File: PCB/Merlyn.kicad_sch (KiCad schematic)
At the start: 92 parts, among them J1 Conn_Coaxial_Small, Q1 JMSL0302AU, Q10 JMSL0302AU, Q11 JMSL0302AU, Q12 JMSL0302AU, Q13 JMSL0302AU, Q14 JMSL0302AU, Q15 JMSL0302AU, Q16 JMSL0302AU, Q17 JMSL0302AU, Q18 JMSL0302AU, Q19 JMSL0302AU, Q2 JMSL0302AU, Q20 JMSL0302AU, Q21 JMSL0302AU, Q22 JMSL0302AU, Q23 JMSL0302AU, Q24 JMSL0302AU, Q3 JMSL0302AU, Q4 JMSL0302AU, Q5 JMSL0302AU, Q6 JMSL0302AU, Q7 JMSL0302AU, Q8 JMSL0302AU, Q9 JMSL0302AU, U1 AT32F435CGU7, U10 JSM6288Q, U11 EFM8BB21F16G-C-QFN20, U12 EFM8BB21F16G-C-QFN20, U13 EFM8BB21F16G-C-QFN20, U14 JSM6288Q, U15 JSM6288Q, U16 JSM6288Q, U17 MPU6500, U18 LMR51420, U2 ESP8285H16, U4 SPX3819, U5 SX1281IMLTRT, U6 W25Q128JVPIM TR, U7 4.7uH, U8 AT7456E, U9 EFM8BB21F16G-C-QFN20, X1 TAXM8M4RDBCCT2T, X2 27MHz, X3 26MHz, X4 52MHz

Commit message: checkpoint
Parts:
- removed Q1, Q10, Q11, Q12, Q13, Q14, Q15, Q16, Q17, Q18, Q19, Q2, Q20, Q21, Q22, Q23, Q24, Q3, Q4, Q5, Q6, Q7, Q8, Q9: JMSL0302AU, easyeda2kicad:DFN-8_L3.2-W3.1-P0.65-LS3.4-BL, symbol Merlyn435:JMSL0302AU
- removed R1: HOYLR2512E-3W-0.5MR-1%, easyeda2kicad:R2512, symbol Merlyn435:HOYLR2512E-3W-0.5MR-1%
- removed U10, U14, U15, U16: JSM6288Q, easyeda2kicad:VQFN-24_L4.0-W4.0-P0.50-TL-EP2.7, symbol Merlyn435:JSM6288Q
- removed U11, U12, U13, U9: EFM8BB21F16G-C-QFN20, easyeda2kicad:QFN-20_L3.0-W3.0-P0.50-BL-EP1.7_EFM8BB21F16G, symbol Merlyn435:EFM8BB21F16G-C-QFN20
- removed U6: W25Q128JVPIM TR, easyeda2kicad:WSON-8_L6.0-W5.0-P1.27-BL-EP, symbol Merlyn435:W25Q128JVPIMTR
- added C31, C32: 10pF, Capacitor_SMD:C_0402_1005Metric, symbol Device:C_Small
- added C33, C34, C35, C36, C37, C39: 0.1uF, Capacitor_SMD:C_0402_1005Metric, symbol Device:C_Small
- added C38: 10uF, Capacitor_SMD:C_0402_1005Metric, symbol Device:C_Small
- added D2, D3: RED, symbol Device:LED_Small
- added R1, R14, R15, R16: 12k, Resistor_SMD:R_0402_1005Metric, symbol Device:R_Small
- added R17, R18: 5.1k, Resistor_SMD:R_0402_1005Metric, symbol Device:R_Small
- added U3: W25Q128JVSIQTR, easyeda2kicad:SOIC-8_L5.3-W5.3-P1.27-LS8.0-BL, symbol Merlyn435:W25Q128JVSIQTR
- C1, C10, C11, C13, C14, C15, C19, C22, C24, C25, C26, C29, C30, C5: LCSC Part C29823 -> C307331
- C16, C17: value 0.1pF -> 10pF
- C2, C3: LCSC Part C96446 -> C96446
- X1: value TAXM8M4RDBCCT2T -> 8MHz
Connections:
- net +3V3: now also U1.1 (VBAT), U1.24 (VDD), U1.36 (VDD), U1.48 (VDD), U1.9 (VDDA/VREF+), C33.2, C34.2, C35.2, C36.2, C38.2, C39.2, R1.1, R16.1, R17.1, R18.1, U3.3 (IO2), U3.7 (IO3), U3.8 (VCC)
- net D+: now also U1.33 (PA12)
- net D-: now also U1.32 (PA11)
- net GND: now also U1.47 (VSS), U1.49 (EP), U1.8 (VSSA/VREF-), X1.2, X1.4, C31.1, C32.1, C33.1, C34.1, C35.1, C36.1, C37.1, C38.1, C39.1, D2.1 (K), R14.2, R15.2, U3.4 (GND)
- net PIN: now also R16.2, U3.1 (~{CS}), U3.2 (DO), U3.5 (DI), U3.6 (CLK)
- net ADC_VOL: now reaches U1.10 (PA0)
- net ADC_CUR: now reaches U1.11 (PA1)
- net UART2_TX: now reaches U1.12 (PA2)
- net UART2_RX: now reaches U1.13 (PA3)
- net SPI1_CS: now reaches U1.14 (PA4)
- net SPI1_SCK: now reaches U1.15 (PA5)
- net SPI1_MISO: now reaches U1.16 (PA6)
- net SPI1_MOSI: now reaches U1.17 (PA7)
- net MOT3: now reaches U1.18 (PB0)
- net MOT4: now reaches U1.19 (PB1)
- net SPI2_CS2: now reaches U1.2 (PC13)
- net BOOT1: now reaches U1.20 (PB2)
- net BOOT1: now also R15.1
- net UART3_TX: now reaches U1.21 (PB10)
- net UART3_RX: now reaches U1.22 (PB11)
- net I2C_SDA: now reaches U1.23 (PH3)
- net SPI2_CS1: now reaches U1.25 (PB12)
- net SPI2_SCK: now reaches U1.26 (PB13)
- net SPI2_MISO: now reaches U1.27 (PB14)
- net SPI2_MOSI: now reaches U1.28 (PB15)
- net LED: now reaches U1.29 (PA8)
- net LED: now also D3.1 (K)
- net UART1_TX: now reaches U1.30 (PA9)
- net UART1_RX: now reaches U1.31 (PA10)
- net SWDIO: now reaches U1.34 (PA13)
- net I2C_SCL: now reaches U1.35 (PH2)
- net SWCLK: now reaches U1.37 (PA14)
- net UART7_RX: now reaches U1.39 (PB3)
- net BEEPER: now reaches U1.4 (PC15)
- net UART7_TX: now reaches U1.40 (PB4)
- net MOT1: now reaches U1.42 (PB6)
- net MOT2: now reaches U1.43 (PB7)
- net BOOT0: now reaches U1.44 (BOOT0)
- net BOOT0: now also R14.1
- net UART5_RX: now reaches U1.45 (PB8)
- net UART5_TX: now reaches U1.46 (PB9)
- net at U1.5 (PH0): now also X1.3, C31.2
- net at U1.6 (PH1): now also X1.1, C32.2
- net NRST: now reaches U1.7 (NRST)
- net NRST: now also C37.2, R1.2
- new net: D3.2 (A), R18.2
- new net: D2.2 (A), R17.2
- no-connect marks 42 -> 44
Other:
- note added: "Flash"
- note added: "MCU"
- moved on the sheet: C1, C10, C11, C12, C13, C14, C15, C16, C17, C18, C19, C2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

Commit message: routing checkpoint
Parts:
- removed D2, D3: RED, symbol Device:LED_Small
- added C40, C41: 0.1uF, Capacitor_SMD:C_0402_1005Metric, symbol Device:C_Small
- added D2: RED, easyeda2kicad:LED0805-RD, symbol Merlyn435:FC-2012HRK-620D
- added D3: GREEN, easyeda2kicad:LED0805-R-RD, symbol Merlyn435:0805G
- added D4: 1N4148W, Diode_SMD:D_SOD-123, symbol Diode:1N4148W
- added H1: ~, easyeda2kicad:Buzzer Pad, symbol Merlyn435:Buzzer
- added H2: ~, easyeda2kicad:JST_SH_SM08B-SRSS-TB_1x08-1MP_P1.00mm_Horizontal, symbol Merlyn435:ESC
- added H3: ~, easyeda2kicad:Camera Pad, symbol Merlyn435:Camera
- added H4: ~, symbol Merlyn435:VTX
- added Q1: 2N7002, Package_TO_SOT_SMD:SOT-23, symbol Transistor_FET:2N7002
- added R19: 12k, Resistor_SMD:R_0402_1005Metric, symbol Device:R_Small
- added R20: 1.5k, Resistor_SMD:R_0402_1005Metric, symbol Device:R_Small
- added R21, R22: 5.1k, Resistor_SMD:R_0402_1005Metric, symbol Device:R_Small
- added U6: BMP388, easyeda2kicad:LGA-10_L2.0-W2.0-P0.50-BL, symbol Merlyn435:BMP388
- USB1: footprint lcsc:USB-C-SMD_TYPE-C-6PIN-2MD-073 -> easyeda2kicad:USB-C-SMD_TYPE-C-6PIN-2MD-073
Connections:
- net +3V3: now also C40.2, C41.2, D4.1 (K), H1.1 (BZ+), R21.2, R22.2, U6.1 (VDDIO), U6.10 (VDD), U6.6 (CSB)
- net +5V: now also H3.1 (5v)
- net ADC_CUR: now also H2.4 (CUR)
- net BEEPER: now also R20.2
- net GND: now also C40.1, C41.1, D2.1 (-), H2.2 (GND), H3.2 (GND), H4.2 (GND), Q1.2 (S), R19.2, U6.3 (GND), U6.5 (SDO), U6.8 (GND), U6.9 (GND)
- net I2C_SCL: now also R21.1, U6.2 (SCL)
- net I2C_SDA: now also R22.1, U6.4 (SDA)
- net LED: now also D3.2 (K)
- net MOT1: now also H2.5 (M1)
- net MOT2: now also H2.6 (M2)
- net MOT3: now also H2.7 (M3)
- net MOT4: now also H2.8 (M4)
- net PIN: now also H4.4 (TX); no longer U17.22 (nCS), U17.23 (SCL/SCLK), U17.24 (SDA/SDI), U17.9 (SDO/AD0), U8.10 (SCLK), U8.11 (SDOUT), U8.8 (~{CS}), U8.9 (SDIN)
- net SPI1_CS: now also U17.22 (nCS)
- net SPI1_MISO: now also U17.9 (SDO/AD0)
- net SPI1_MOSI: now also U17.24 (SDA/SDI)
- net SPI1_SCK: now also U17.23 (SCL/SCLK)
- net SPI2_CS1: now also U8.8 (~{CS})
- net SPI2_MISO: now also U8.11 (SDOUT)
- net SPI2_MOSI: now also U8.9 (SDIN)
- net SPI2_SCK: now also U8.10 (SCLK)
- net VBAT: now also H2.1 (BAT+), H4.1 (BAT+)
- net VIDIN: now also H3.3 (VID_IN)
- net VIDOUT: now also H4.3 (VID_OUT)
- net at R18.2: now also D3.1 (A)
- net at R17.2: now also D2.2 (+)
- new net: D4.2 (A), H1.2 (BZ-), Q1.3 (D)
- new net: Q1.1 (G), R19.1, R20.1
- no-connect marks 44 -> 46
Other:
- moved on the sheet: C25, C9, R18, X2

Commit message: checkpoint
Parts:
- H2: footprint easyeda2kicad:JST_SH_SM08B-SRSS-TB_1x08-1MP_P1.00mm_Horizontal -> easyeda2kicad:ESC Header
- USB1: footprint easyeda2kicad:USB-C-SMD_TYPE-C-6PIN-2MD-073 -> easyeda2kicad:USB-TYPE-C-SMD_TYPE-C-16P-QTWT
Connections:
- net D+: now also D1.4; no longer D1.6
- net D-: now also D1.6; no longer D1.4
- net DIN+: now also D1.3; no longer D1.1
- net DIN-: now also D1.1; no longer D1.3
- net PIN: no longer R16.2, U2.25 (U0RXD), U2.26 (U0TXD), U3.1 (~{CS}), U3.2 (DO), U3.5 (DI), U3.6 (CLK)
- net SPI2_CS2: now also R16.2, U3.1 (~{CS})
- net SPI2_MISO: now also U3.2 (DO)
- net SPI2_MOSI: now also U3.5 (DI)
- net SPI2_SCK: now also U3.6 (CLK)
- net UART2_RX: now also U2.26 (U0TXD)
- net UART2_TX: now also U2.25 (U0RXD)
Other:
- moved on the sheet: C16, C38, C39

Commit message: checkpoint
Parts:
- added C42: 0.1uF, Capacitor_SMD:C_0402_1005Metric, symbol Device:C_Small
- added R23: 91k, Resistor_SMD:R_0603_1608Metric, symbol Device:R_Small
- added R25: 12k, Resistor_SMD:R_0402_1005Metric, symbol Device:R_Small
- H4: footprint (none) -> easyeda2kicad:VTX Pad
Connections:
- net PIN is gone; now on net UART1_TX: H4.4 (TX)
- net ADC_VOL: now also C42.2, R23.2, R25.1
- net GND: now also C42.1, R25.2
- net VBAT: now also R23.1

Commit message: polka dots
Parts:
- added H10: ~, easyeda2kicad:SWCLK TP, symbol Merlyn435:SWCLK
- added H11: ~, easyeda2kicad:SWDIO TP, symbol Merlyn435:SWDIO
- added H12: ~, easyeda2kicad:SWD_BOOT TP, symbol Merlyn435:SWD_BOOT
- added H13: ~, easyeda2kicad:SWD_RST TP, symbol Merlyn435:SWD_RST
- added H14: ~, easyeda2kicad:Power Pad, symbol Merlyn435:Power
- added H5: ~, easyeda2kicad:GPS Pad, symbol Merlyn435:GPS
- added H6: ~, easyeda2kicad:UART5 PAD, symbol Merlyn435:UART5
- added H7: ~, easyeda2kicad:UART3 PAD, symbol Merlyn435:UART5
- added H8: ~, easyeda2kicad:ELRS_RX TP, symbol Merlyn435:ELRX_RX
- added H9: ~, easyeda2kicad:ELRS_TX TP, symbol Merlyn435:ELRX_TX
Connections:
- net +3V3: now also H14.3 (3v3)
- net +5V: now also H14.1 (5v), H5.1 (5v), H6.1 (5v), H7.1 (5v)
- net BOOT0: now also H12.1 (BOOT)
- net GND: now also H14.2 (GND), H5.2 (GND), H6.2 (GND), H7.2 (GND)
- net I2C_SCL: now also H5.6 (SCL)
- net I2C_SDA: now also H5.5 (SDA)
- net NRST: now also H13.1 (RST)
- net SWCLK: now also H10.1 (SWCLK)
- net SWDIO: now also H11.1 (SWDIO)
- net UART2_RX: now also H9.1 (TX)
- net UART2_TX: now also H8.1 (RX)
- net UART3_RX: now also H7.3 (RX)
- net UART3_TX: now also H7.4 (TX)
- net UART5_RX: now also H6.3 (RX)
- net UART5_TX: now also H6.4 (TX)
- net UART7_RX: now also H5.3 (RX)
- net UART7_TX: now also H5.4 (TX)
- no-connect marks 46 -> 48

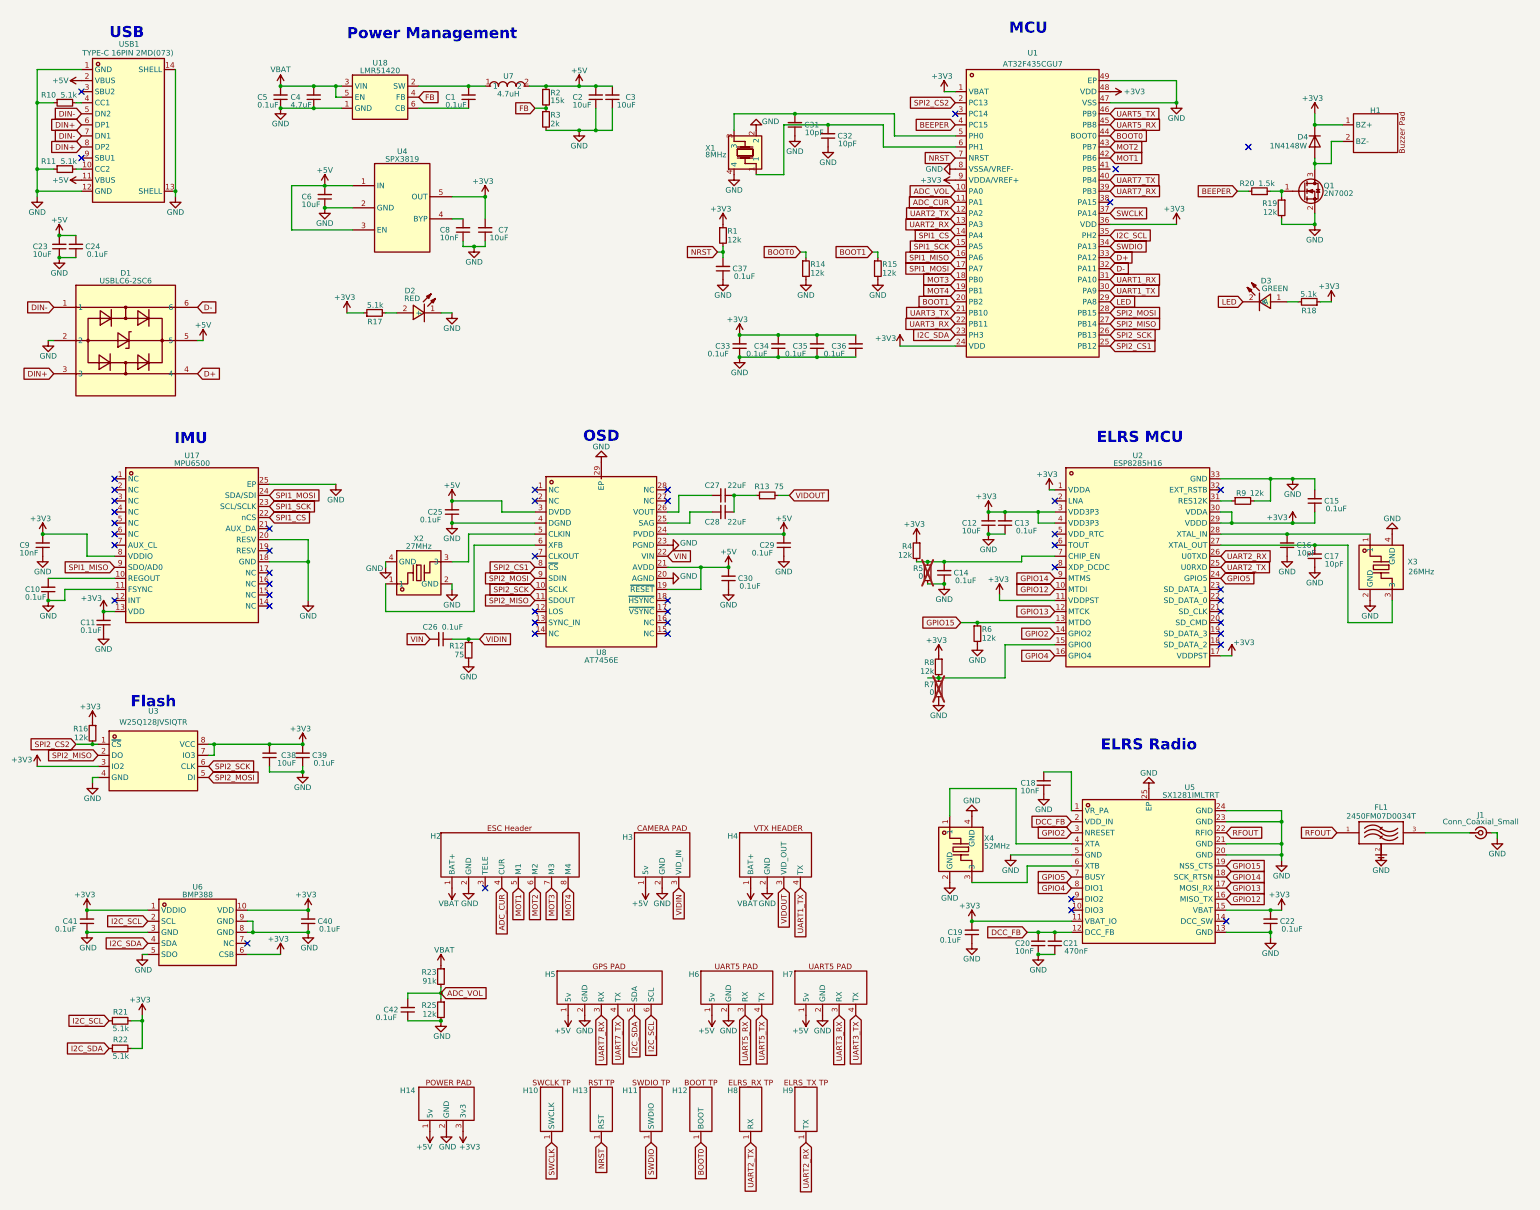
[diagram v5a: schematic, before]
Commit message: completed flight controller
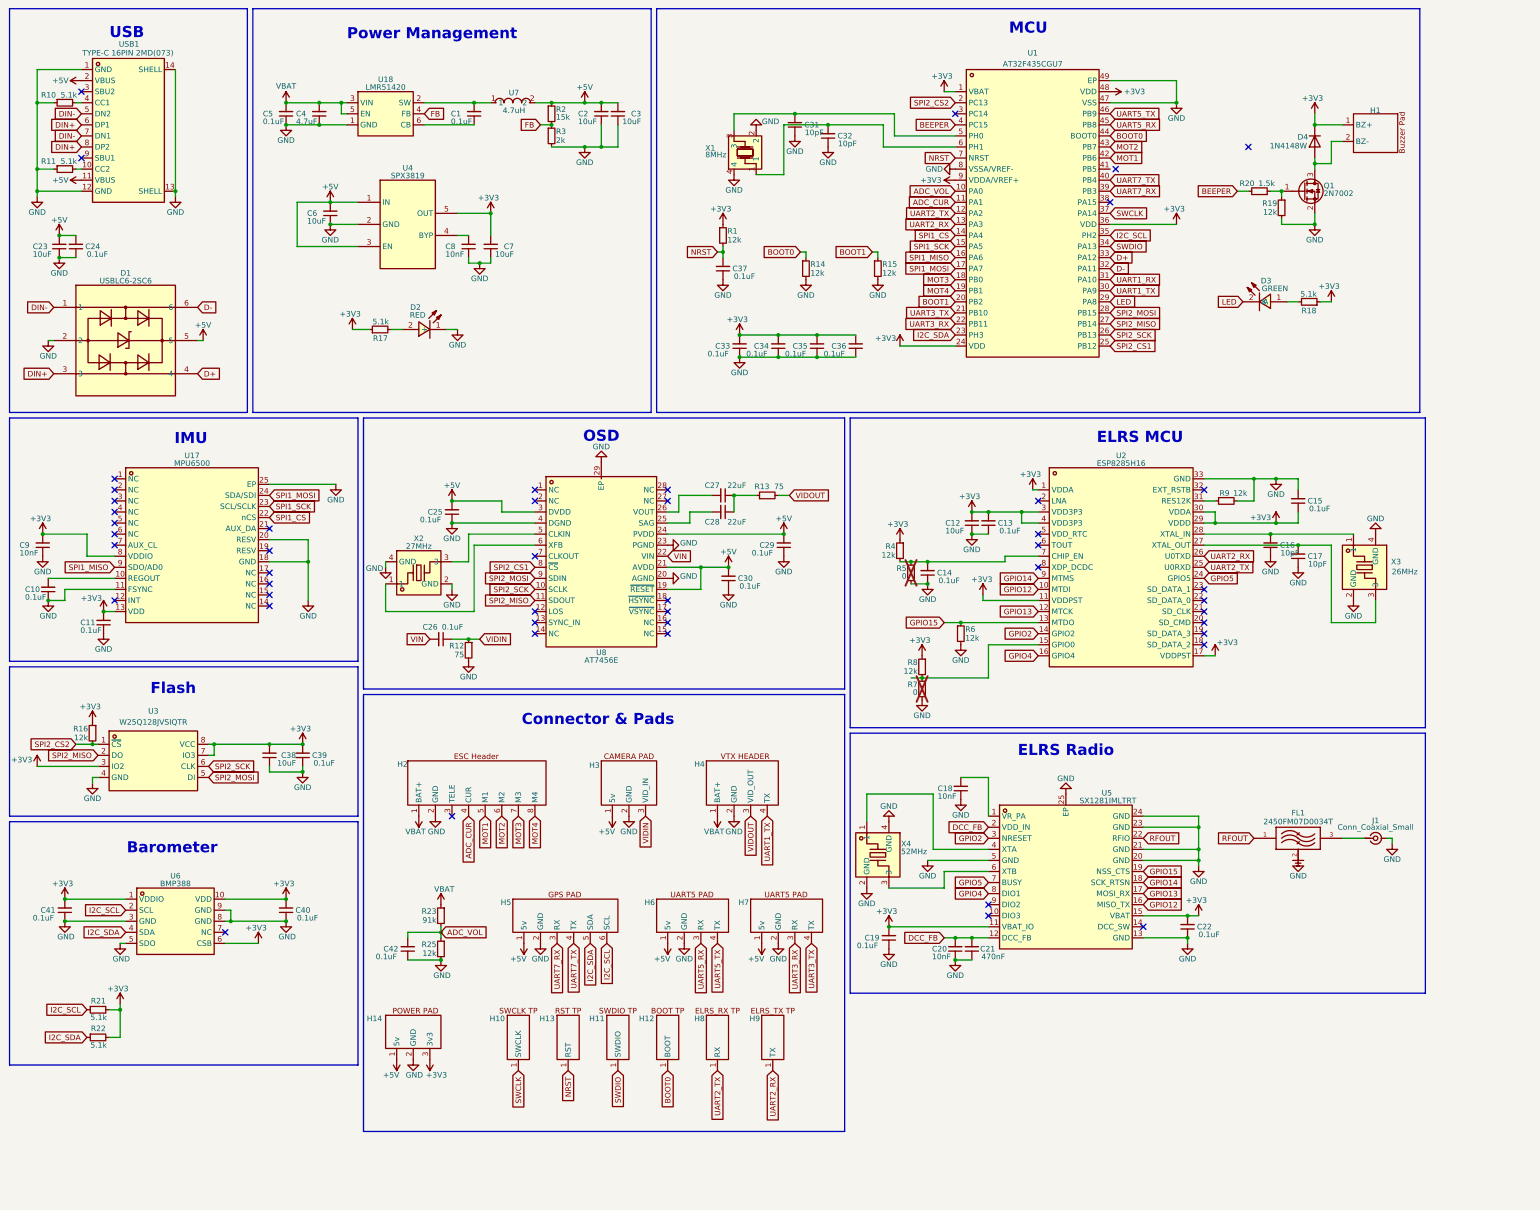
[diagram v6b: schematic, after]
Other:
- note added: "Barometer"
- note added: "Connector & Pads"
- moved on the sheet: C1, C12, C13, C14, C15, C16, C17, C18, C19, C2, C20, C21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
